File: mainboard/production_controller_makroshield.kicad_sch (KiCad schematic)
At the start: 45 parts, among them J1 CON_TERM_BLK_1X2_TB008A-508-0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, J2 CON_HDR_MIKROBUS_ADDON_TH, J3 CON_HDR_MIKROBUS_SOCKET_TH, Q1 TRX_PMOS_AOD4189, Q2 TRX_NPN_MMBT3904-TP, U1 IO_EXP_PI4IOE5V6416ZDEX, U2 IO_EXP_PI4IOE5V6416ZDEX, U3 CON_BARREL_2.1X5.5_PJ-002A, U4 SUN_CUR_ACS711KEXLT-31AB-T, U5 ADC_NAU7802SGI

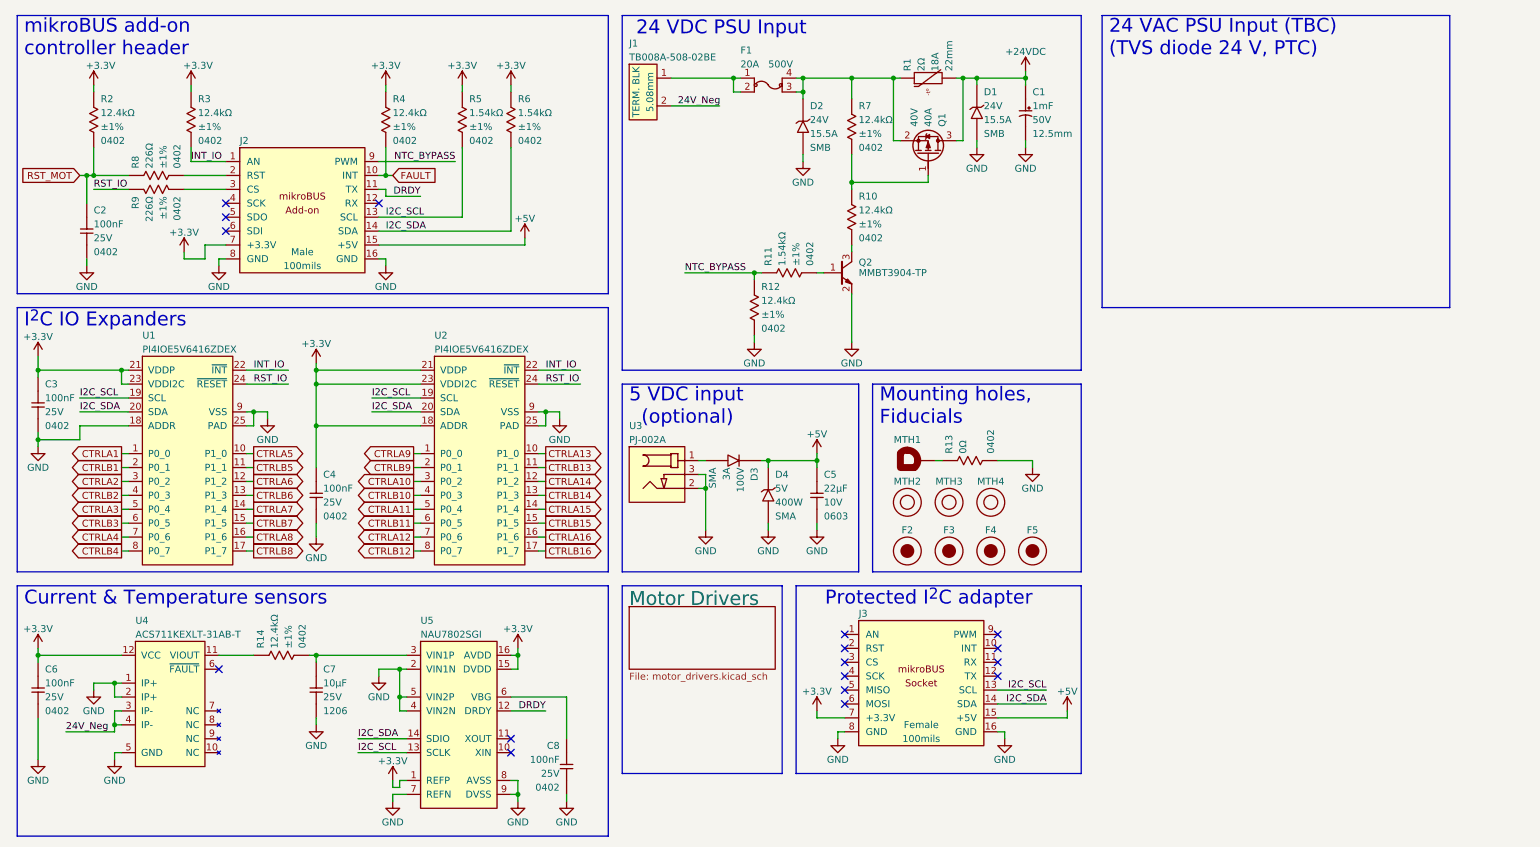
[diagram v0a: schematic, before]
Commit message: rename project, comple simple switch layout, fix thermal reliefs
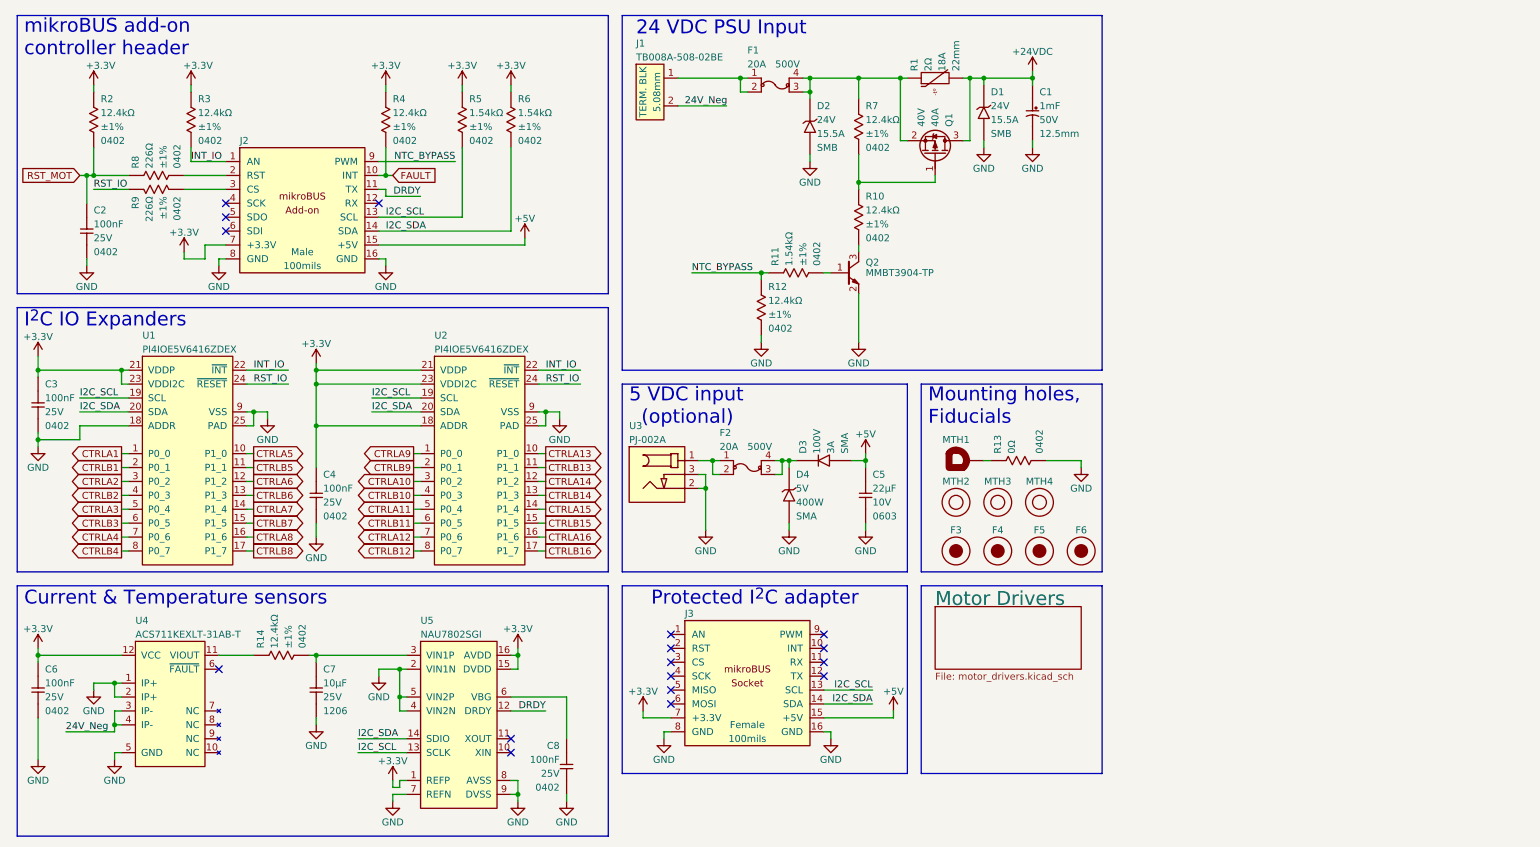
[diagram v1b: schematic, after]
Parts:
- added F2: FUS_BLADE_MINI_3588-1, connaxio-connectors:FUS_BLADE_MINI_3588-1, symbol connaxio-connectors:FUS_BLADE_MINI_3588-1
- renumbered F2 to F3, F3 to F4, F4 to F5, F5 to F6
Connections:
- net +5V: now also D3.2 (A); no longer D3.1 (K), D4.1 (K)
- net at U3.1: now also F2.1, F2.2; no longer D3.2 (A)
- new net: D3.1 (K), D4.1 (K), F2.3, F2.4
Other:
- note removed: "24 VAC PSU Input (TBC) (TVS diode 24 V, PTC)"
- moved on the sheet: C1, C5, D1, D2, D3, F1, F3, F4, F5, F6, J1, J3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

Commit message: Inverted motor controls for open-drain operation and manual switch override compatibility
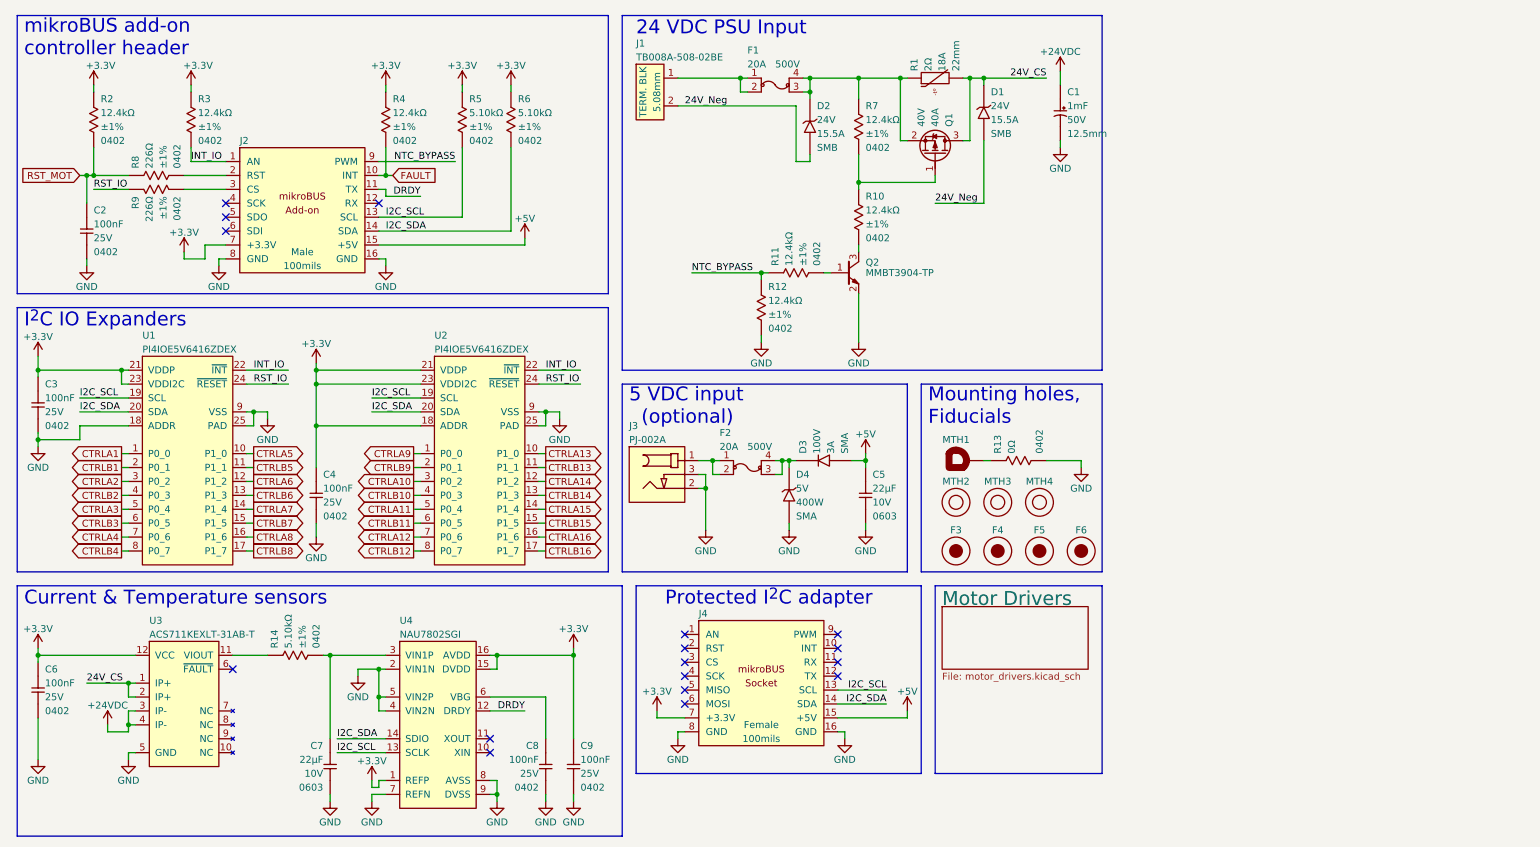
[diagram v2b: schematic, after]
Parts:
- removed C7: CAP_CER_10UF_25V_1206, connaxio-capacitors:CAP_CER_1206_3216M, symbol connaxio-capacitors:CAP_CER_10UF_25V_1206
- removed R11, R5, R6: RES_1.54KΩ_1%_0402, connaxio-resistors:RES_0402_1005M, symbol connaxio-resistors:RES_1.54KΩ_1%_0402
- removed R14: RES_12.4KΩ_1%_0402, connaxio-resistors:RES_0402_1005M, symbol connaxio-resistors:RES_12.4KΩ_1%_0402
- added C7: CAP_CER_22UF_10V_0603, connaxio-capacitors:CAP_CER_0603_1608M, symbol connaxio-capacitors:CAP_CER_22UF_10V_0603
- added C9: CAP_CER_100NF_25V_0402, connaxio-capacitors:CAP_CER_0402_1005M, symbol connaxio-capacitors:CAP_CER_100NF_25V_0402
- added R11: RES_12.4KΩ_1%_0402, connaxio-resistors:RES_0402_1005M, symbol connaxio-resistors:RES_12.4KΩ_1%_0402
- added R14, R5, R6: RES_5.10KΩ_1%_0402, connaxio-resistors:RES_0402_1005M, symbol connaxio-resistors:RES_5.10KΩ_1%_0402
- renumbered U3 to J3, J3 to J4, U4 to U3, U5 to U4
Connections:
- net +24VDC: now also U3.3 (IP-), U3.4 (IP-); no longer D1.1 (K), Q1.3 (D), R1.2
- net +3.3V: now also C9.1, R5.1, R6.1
- net 24V_Neg: now also D1.2 (A), D2.2 (A); no longer U3.3 (IP-), U3.4 (IP-)
- net GND: now also C7.2, C9.2; no longer D1.2 (A), D2.2 (A), U3.1 (IP+), U3.2 (IP+)
- net I2C_SCL: now also R5.2
- net I2C_SDA: now also R6.2
- net NTC_BYPASS: now also R11.1
- net at Q2.1 (B): now also R11.2
- net at U4.3 (VIN1P): now also C7.1, R14.2
- net at U3.11 (VIOUT): now also R14.1
- new net 24V_CS: D1.1 (K), Q1.3 (D), R1.2, U3.1 (IP+), U3.2 (IP+)
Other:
- moved on the sheet: C1, C8, J4, U3, U4

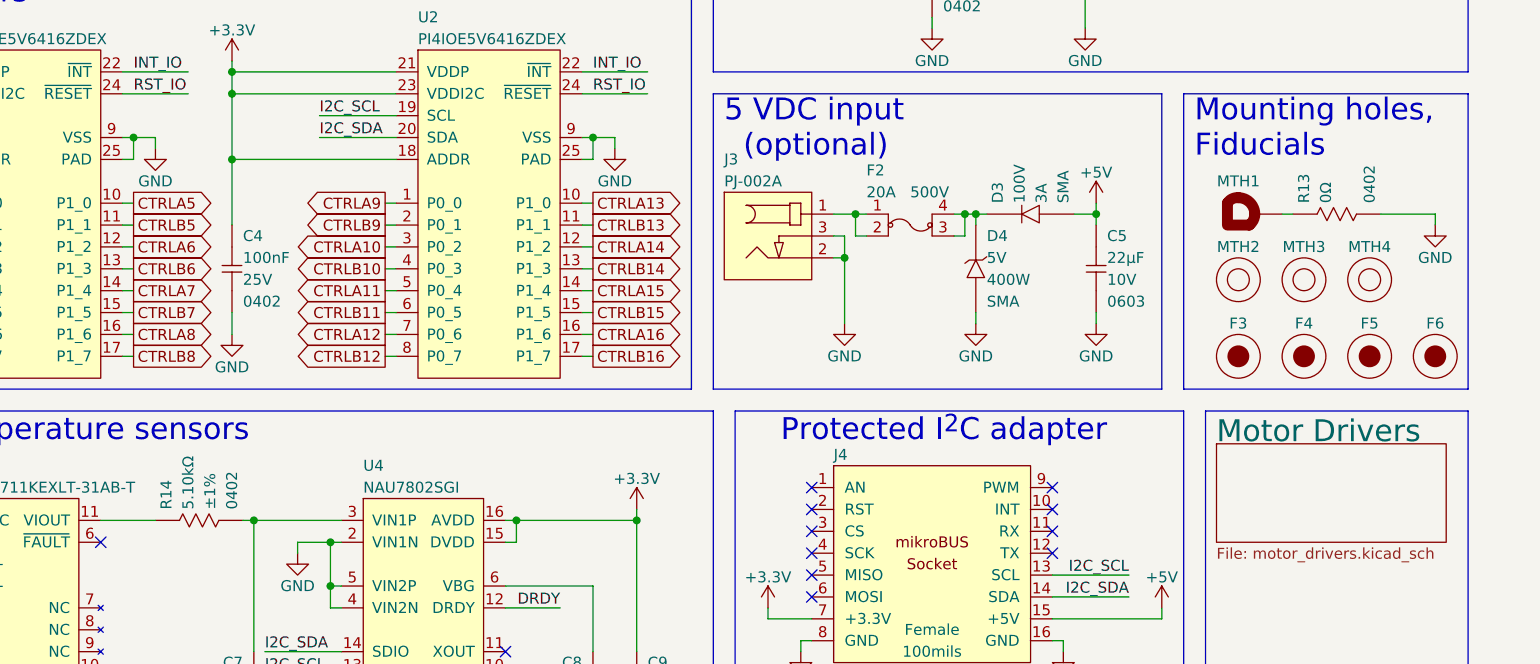
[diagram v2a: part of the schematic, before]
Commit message: Position drive rmodules, choose enclosure, shape PCB
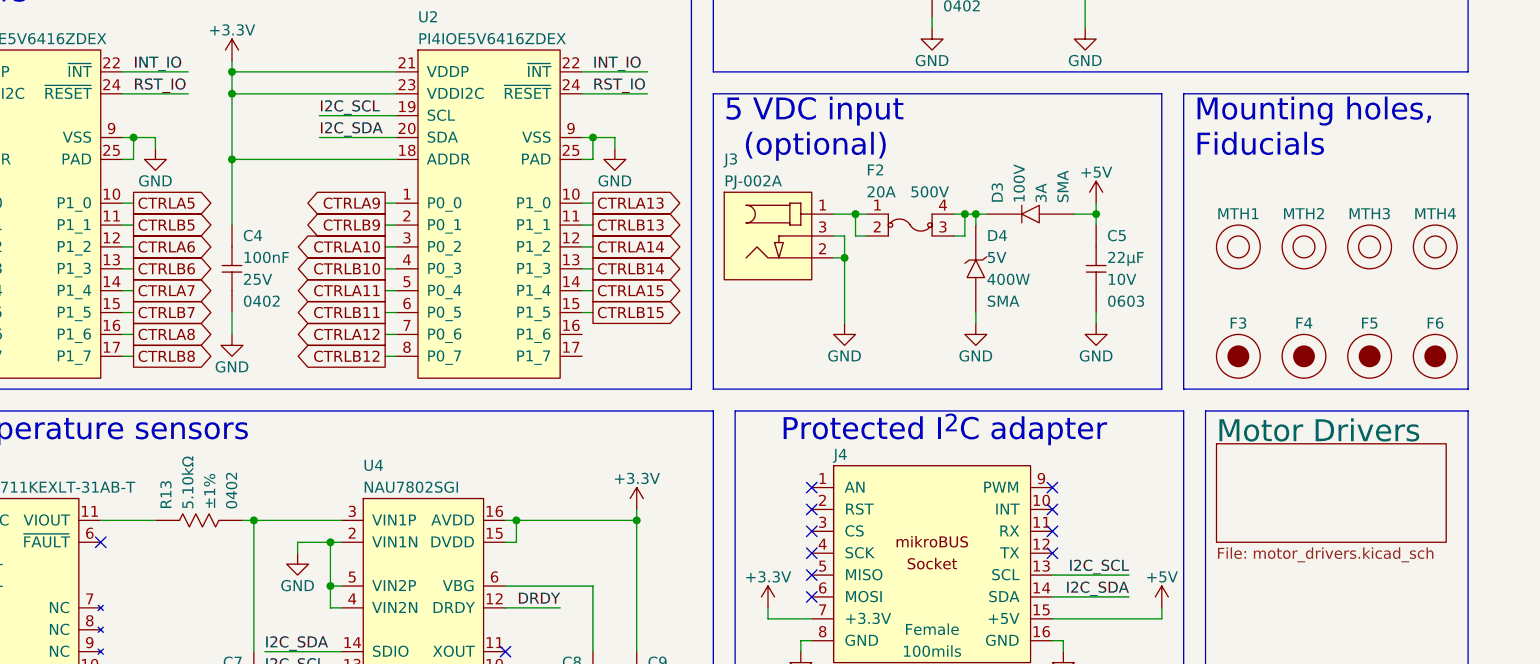
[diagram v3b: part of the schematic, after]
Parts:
- removed MTH1: MTH_M2.5_PTH_CORNER, connaxio-mechanical:MTH_M2.5_PTH_CORNER, symbol connaxio-mechanical:MTH_M2.5_PTH_CORNER
- removed MTH2, MTH3, MTH4: MTH_M2.5_NPTH, connaxio-mechanical:MTH_M2.5_NPTH, symbol connaxio-mechanical:MTH_M2.5_NPTH
- removed R13: RES_0Ω_0402, connaxio-resistors:RES_0402_1005M, symbol connaxio-resistors:RES_0Ω_0402
- added MTH1, MTH2, MTH3, MTH4: MTH_M5_NPTH, connaxio-mechanical:MTH_M5_NPTH, symbol connaxio-mechanical:MTH_M5_NPTH
- renumbered R14 to R13
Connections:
- net CTRLA16: no longer names the net of U2.16 (P1_6)
- net CTRLB16: no longer names the net of U2.17 (P1_7)

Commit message: Routing mainboard
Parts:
- removed J3: CON_BARREL_2.1X5.5_PJ-002A, connaxio-connectors:CON_BARREL_2.1X5.5_PJ-002A, symbol connaxio-connectors:CON_BARREL_2.1X5.5_PJ-002A
- added F2: FUS_BLADE_MINI_3588-1, connaxio-connectors:FUS_BLADE_MINI_3588-1, symbol connaxio-connectors:FUS_BLADE_MINI_3588-1
- added J2, J4: CON_TERM_BLK_1X2_TB008A-508-02BE, connaxio-connectors:CON_TERM_BLK_1X2_TB008A-508-02BE, symbol connaxio-connectors:CON_TERM_BLK_1X2_TB008A-508-02BE
- renumbered F2 to F3, F3 to F4, F4 to F5, F5 to F6, F6 to F7, J2 to J3, J4 to J5
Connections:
- net 24V_Neg is gone; now on net GND: D1.2 (A), D2.2 (A), J1.2
- net +24VDC: now also D1.1 (K), U3.1 (IP+), U3.2 (IP+), F2.1, F2.2; no longer U3.3 (IP-), U3.4 (IP-)
- net +5V: now also D3.1 (K); no longer D3.2 (A)
- net GND: now also J2.2, J4.2
- net at D4.1 (K), F3.3, F3.4: now also D3.2 (A); no longer D3.1 (K)
- net at F3.1, F3.2: now also J4.1
- removed net 24V_CS: D1.1 (K), Q1.3 (D), R1.2, U3.1 (IP+), U3.2 (IP+)
- new net: F2.3, F2.4, J2.1
- new net CS+: Q1.3 (D), R1.2, U3.3 (IP-), U3.4 (IP-)
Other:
- note added: "Reverse current slope for better PCB layout"
- moved on the sheet: C5, D2, D3, D4, F1, F3, F4, F5, F6, F7, J1, MTH1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

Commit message: DRC pass
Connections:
- net CTRLA1: now also U1.10 (P1_0); no longer U1.1 (P0_0)
- net CTRLA10: now also U2.12 (P1_2); no longer U2.3 (P0_2)
- net CTRLA11: now also U2.14 (P1_4); no longer U2.5 (P0_4)
- net CTRLA12: now also U2.16 (P1_6); no longer U2.7 (P0_6)
- net CTRLA13: now also U2.3 (P0_2); no longer U2.10 (P1_0)
- net CTRLA14: now also U2.5 (P0_4); no longer U2.12 (P1_2)
- net CTRLA15: now also U2.7 (P0_6); no longer U2.14 (P1_4)
- net CTRLA2: now also U1.12 (P1_2); no longer U1.3 (P0_2)
- net CTRLA3: now also U1.14 (P1_4); no longer U1.5 (P0_4)
- net CTRLA4: now also U1.16 (P1_6); no longer U1.7 (P0_6)
- net CTRLA5: now also U1.1 (P0_0); no longer U1.10 (P1_0)
- net CTRLA6: now also U1.3 (P0_2); no longer U1.12 (P1_2)
- net CTRLA7: now also U1.5 (P0_4); no longer U1.14 (P1_4)
- net CTRLA8: now also U1.7 (P0_6); no longer U1.16 (P1_6)
- net CTRLA9: now also U2.10 (P1_0); no longer U2.1 (P0_0)
- net CTRLB1: now also U1.11 (P1_1); no longer U1.2 (P0_1)
- net CTRLB10: now also U2.13 (P1_3); no longer U2.4 (P0_3)
- net CTRLB11: now also U2.15 (P1_5); no longer U2.6 (P0_5)
- net CTRLB12: now also U2.17 (P1_7); no longer U2.8 (P0_7)
- net CTRLB13: now also U2.4 (P0_3); no longer U2.11 (P1_1)
- net CTRLB14: now also U2.6 (P0_5); no longer U2.13 (P1_3)
- net CTRLB15: now also U2.8 (P0_7); no longer U2.15 (P1_5)
- net CTRLB2: now also U1.13 (P1_3); no longer U1.4 (P0_3)
- net CTRLB3: now also U1.15 (P1_5); no longer U1.6 (P0_5)
- net CTRLB4: now also U1.17 (P1_7); no longer U1.8 (P0_7)
- net CTRLB5: now also U1.2 (P0_1); no longer U1.11 (P1_1)
- net CTRLB6: now also U1.4 (P0_3); no longer U1.13 (P1_3)
- net CTRLB7: now also U1.6 (P0_5); no longer U1.15 (P1_5)
- net CTRLB8: now also U1.8 (P0_7); no longer U1.17 (P1_7)
- net CTRLB9: now also U2.11 (P1_1); no longer U2.2 (P0_1)
- no-connect marks 17 -> 19
